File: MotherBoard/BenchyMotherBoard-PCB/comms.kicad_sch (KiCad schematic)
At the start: 0 parts

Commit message: Add MORE regulators, USB, Display, and SDCard
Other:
- company: (none) -> Daxxn Industries
- title: (none) -> Benchy Version 2
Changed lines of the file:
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@@
 (kicad_sch (version 20211123) (generator eeschema)
-  (paper "A4")
+  (paper "A2")
+  (title_block
+    (title "Benchy Version 2")
+    (rev "REV1")
+    (company "Daxxn Industries")
+  )
 )

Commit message: Initial schematic lock
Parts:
- added C? (x4): 10uF, Capacitor_SMD:C_1210_3225Metric, symbol Device:C_Small
- added D? (x6): GP DIODE, Diode_SMD:D_SOD-123, symbol Device:D_Small
- added J?: COMMS-ELOAD, Connector_JST:JST_XA_B04B-XASK-1_1x04_P2.50mm_Vertical, symbol Connector:Conn_01x04_Male
- added J?: COMMS-PWR, Connector_JST:JST_XA_B04B-XASK-1_1x04_P2.50mm_Vertical, symbol Connector:Conn_01x04_Male
- added J?: COMMS-RELAY, Connector_JST:JST_XA_B04B-XASK-1_1x04_P2.50mm_Vertical, symbol Connector:Conn_01x04_Male
- added J?: COMMS-LOGIC, Connector_JST:JST_XA_B04B-XASK-1_1x04_P2.50mm_Vertical, symbol Connector:Conn_01x04_Male
- added K? (x6): JW2SN, Relay_THT:Relay_DPDT_Panasonic_JW2, symbol Daxxn_Relays:JW2SN
- added Q? (x6): MMBT2222A, Package_TO_SOT_SMD:SOT-23, symbol Daxxn_Transistors:MMBT2222A
- added Q? (x6): SSM3K361R_SOT23F, Package_TO_SOT_SMD:SOT-23, symbol Daxxn_Transistors:SSM3K361R_SOT23F
- added R? (x6): 10K, Resistor_SMD:R_0402_1005Metric, symbol Device:R_Small_US
- added R? (x6): 100, Resistor_SMD:R_0402_1005Metric, symbol Device:R_Small_US
- added R? (x6): 1K, Resistor_SMD:R_0402_1005Metric, symbol Device:R_Small_US
- added U?: MAINS-OUT-2, Daxxn_Connectors:AC-EARTH-DIRECT-WIRE, symbol Daxxn_Connectors:3-PIN-AC-DIRECT
- added U?: MAINS-OUT-6, Daxxn_Connectors:AC-EARTH-DIRECT-WIRE, symbol Daxxn_Connectors:3-PIN-AC-DIRECT
- added U?: MAINS-OUT-5, Daxxn_Connectors:AC-EARTH-DIRECT-WIRE, symbol Daxxn_Connectors:3-PIN-AC-DIRECT
- added U?: MAINS-OUT-1, Daxxn_Connectors:AC-EARTH-DIRECT-WIRE, symbol Daxxn_Connectors:3-PIN-AC-DIRECT
- added U?: MAINS-OUT-4, Daxxn_Connectors:AC-EARTH-DIRECT-WIRE, symbol Daxxn_Connectors:3-PIN-AC-DIRECT
- added U?: MAINS-OUT-3, Daxxn_Connectors:AC-EARTH-DIRECT-WIRE, symbol Daxxn_Connectors:3-PIN-AC-DIRECT
- added U?: MAINS-IN, Daxxn_Connectors:AC-EARTH-DIRECT-WIRE, symbol Daxxn_Connectors:3-PIN-AC-DIRECT
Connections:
- new net: Q?.3 (C), R?.1, R?.1 (x6)
- new net: Q?.1 (G), R?.2 (x6)
- new net: D?.2 (A), K?.C-, Q?.3 (D) (x6)
- new net: Q?.2 (B), R?.1 (x6)
- new net: K?.NO2, U?.1 (P) (x6)
- new net: K?.NO1, U?.2 (N) (x6)
- new net: K?.COM1, K?.COM1, K?.COM1, K?.COM1, K?.COM1, K?.COM1, U?.2 (N)
- new net: K?.COM2, K?.COM2, K?.COM2, K?.COM2, K?.COM2, K?.COM2, U?.1 (P)
- new net COMMS.ELOAD-SCK: J?.3 (Pin_3)
- new net COMMS.ELOAD-SDA: J?.2 (Pin_2)
- new net COMMS.LOGIC-SCK: J?.3 (Pin_3)
- new net COMMS.LOGIC-SDA: J?.2 (Pin_2)
- new net COMMS.MAINS-1: R?.2
- new net COMMS.MAINS-2: R?.2
- new net COMMS.MAINS-3: R?.2
- new net COMMS.MAINS-4: R?.2
- new net COMMS.MAINS-5: R?.2
- new net COMMS.MAINS-6: R?.2
- new net COMMS.PWR-SCK: J?.3 (Pin_3)
- new net COMMS.PWR-SDA: J?.2 (Pin_2)
- new net COMMS.RELAY-SCK: J?.3 (Pin_3)
- new net COMMS.RELAY-SDA: J?.2 (Pin_2)
- new net GND: C?.2, C?.2, C?.2, C?.2, J?.4 (Pin_4), J?.4 (Pin_4), J?.4 (Pin_4), J?.4 (Pin_4), Q?.1 (E), Q?.1 (E), Q?.1 (E), Q?.1 (E), Q?.1 (E), Q?.1 (E), Q?.2 (S), Q?.2 (S), Q?.2 (S), Q?.2 (S), Q?.2 (S), Q?.2 (S), U?.3 (E), U?.3 (E), U?.3 (E), U?.3 (E), U?.3 (E), U?.3 (E), U?.3 (E)
- new net VCC: D?.1 (K), D?.1 (K), D?.1 (K), D?.1 (K), D?.1 (K), D?.1 (K), K?.C+, K?.C+, K?.C+, K?.C+, K?.C+, K?.C+, R?.2, R?.2, R?.2, R?.2, R?.2, R?.2
- new net VDD: C?.1, C?.1, C?.1, C?.1, J?.1 (Pin_1), J?.1 (Pin_1), J?.1 (Pin_1), J?.1 (Pin_1)
- no-connect marks 0 -> 12

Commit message: (WIP) Start layout
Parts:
- gave numbers to parts that had none: 57
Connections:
- net VCC: now also K1.8, K2.8, K3.8, K4.8, K5.8, K6.8; no longer K1.C+, K2.C+, K3.C+, K4.C+, K5.C+, K6.C+
- net at D11.2 (A), Q8.3 (D): now also K3.1; no longer K3.C-
- net at D10.2 (A), Q6.3 (D): now also K2.1; no longer K2.C-
- net at U22.1 (P): now also K2.5; no longer K2.NO2
- net at U22.2 (N): now also K2.4; no longer K2.NO1
- net at U26.1 (P): now also K6.5; no longer K6.NO2
- net at U26.2 (N): now also K6.4; no longer K6.NO1
- net at D14.2 (A), Q14.3 (D): now also K6.1; no longer K6.C-
- net at D13.2 (A), Q12.3 (D): now also K5.1; no longer K5.C-
- net at D12.2 (A), Q10.3 (D): now also K4.1; no longer K4.C-
- net at U24.2 (N): now also K4.4; no longer K4.NO1
- net at U24.1 (P): now also K4.5; no longer K4.NO2
- net at U25.2 (N): now also K5.4; no longer K5.NO1
- net at U25.1 (P): now also K5.5; no longer K5.NO2
- net at D9.2 (A), Q4.3 (D): now also K1.1; no longer K1.C-
- net at U20.2 (N): now also K1.4; no longer K1.NO1
- net at U20.1 (P): now also K1.5; no longer K1.NO2
- net at U23.2 (N): now also K3.4; no longer K3.NO1
- net at U23.1 (P): now also K3.5; no longer K3.NO2
- new net: K1.3, K2.3, K3.3, K4.3, K5.3, K6.3, U21.2 (N)
- new net: K1.6, K2.6, K3.6, K4.6, K5.6, K6.6, U21.1 (P)
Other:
- title: Benchy Version 2 -> Benchy Reloaded

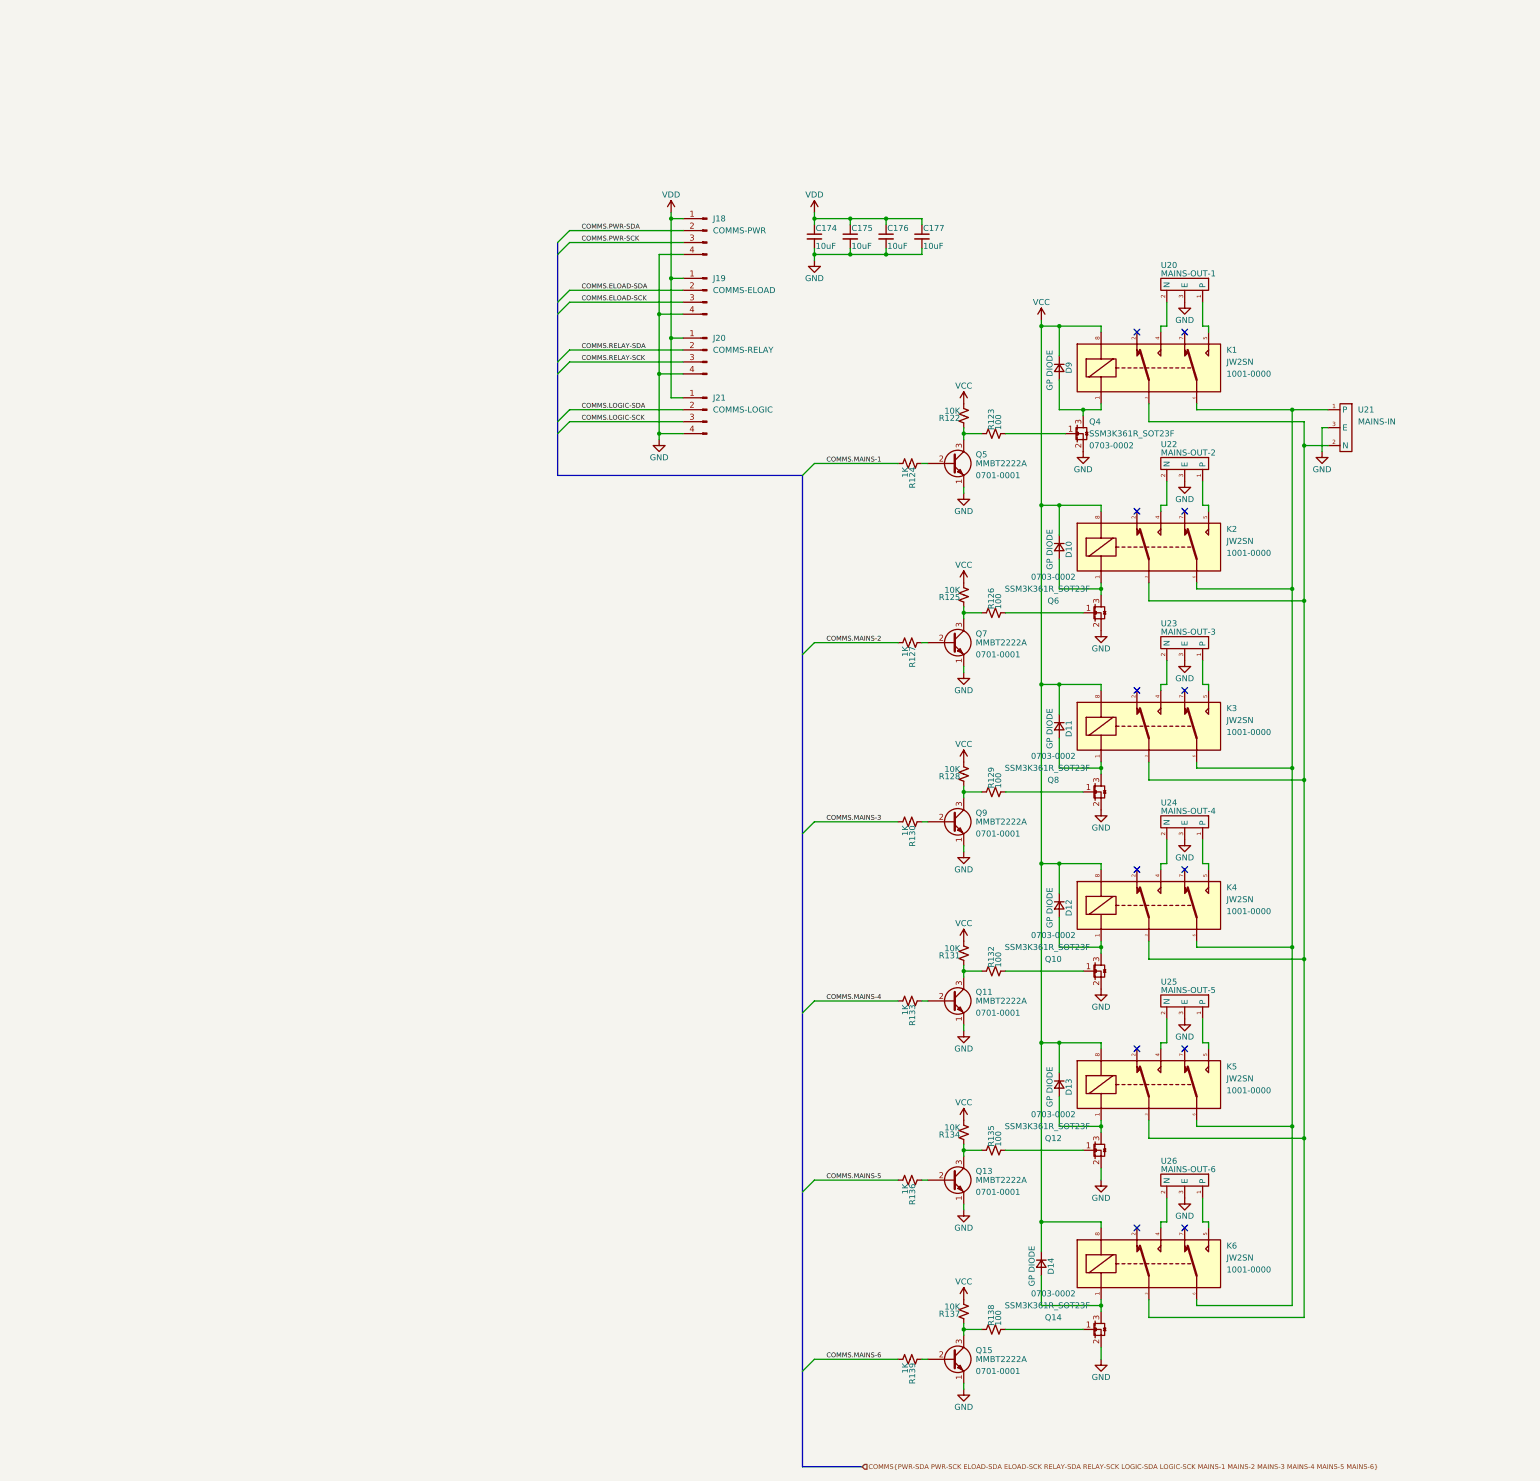
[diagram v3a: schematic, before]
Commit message: (WIP) Replaced DDR VRef with reg and started layout
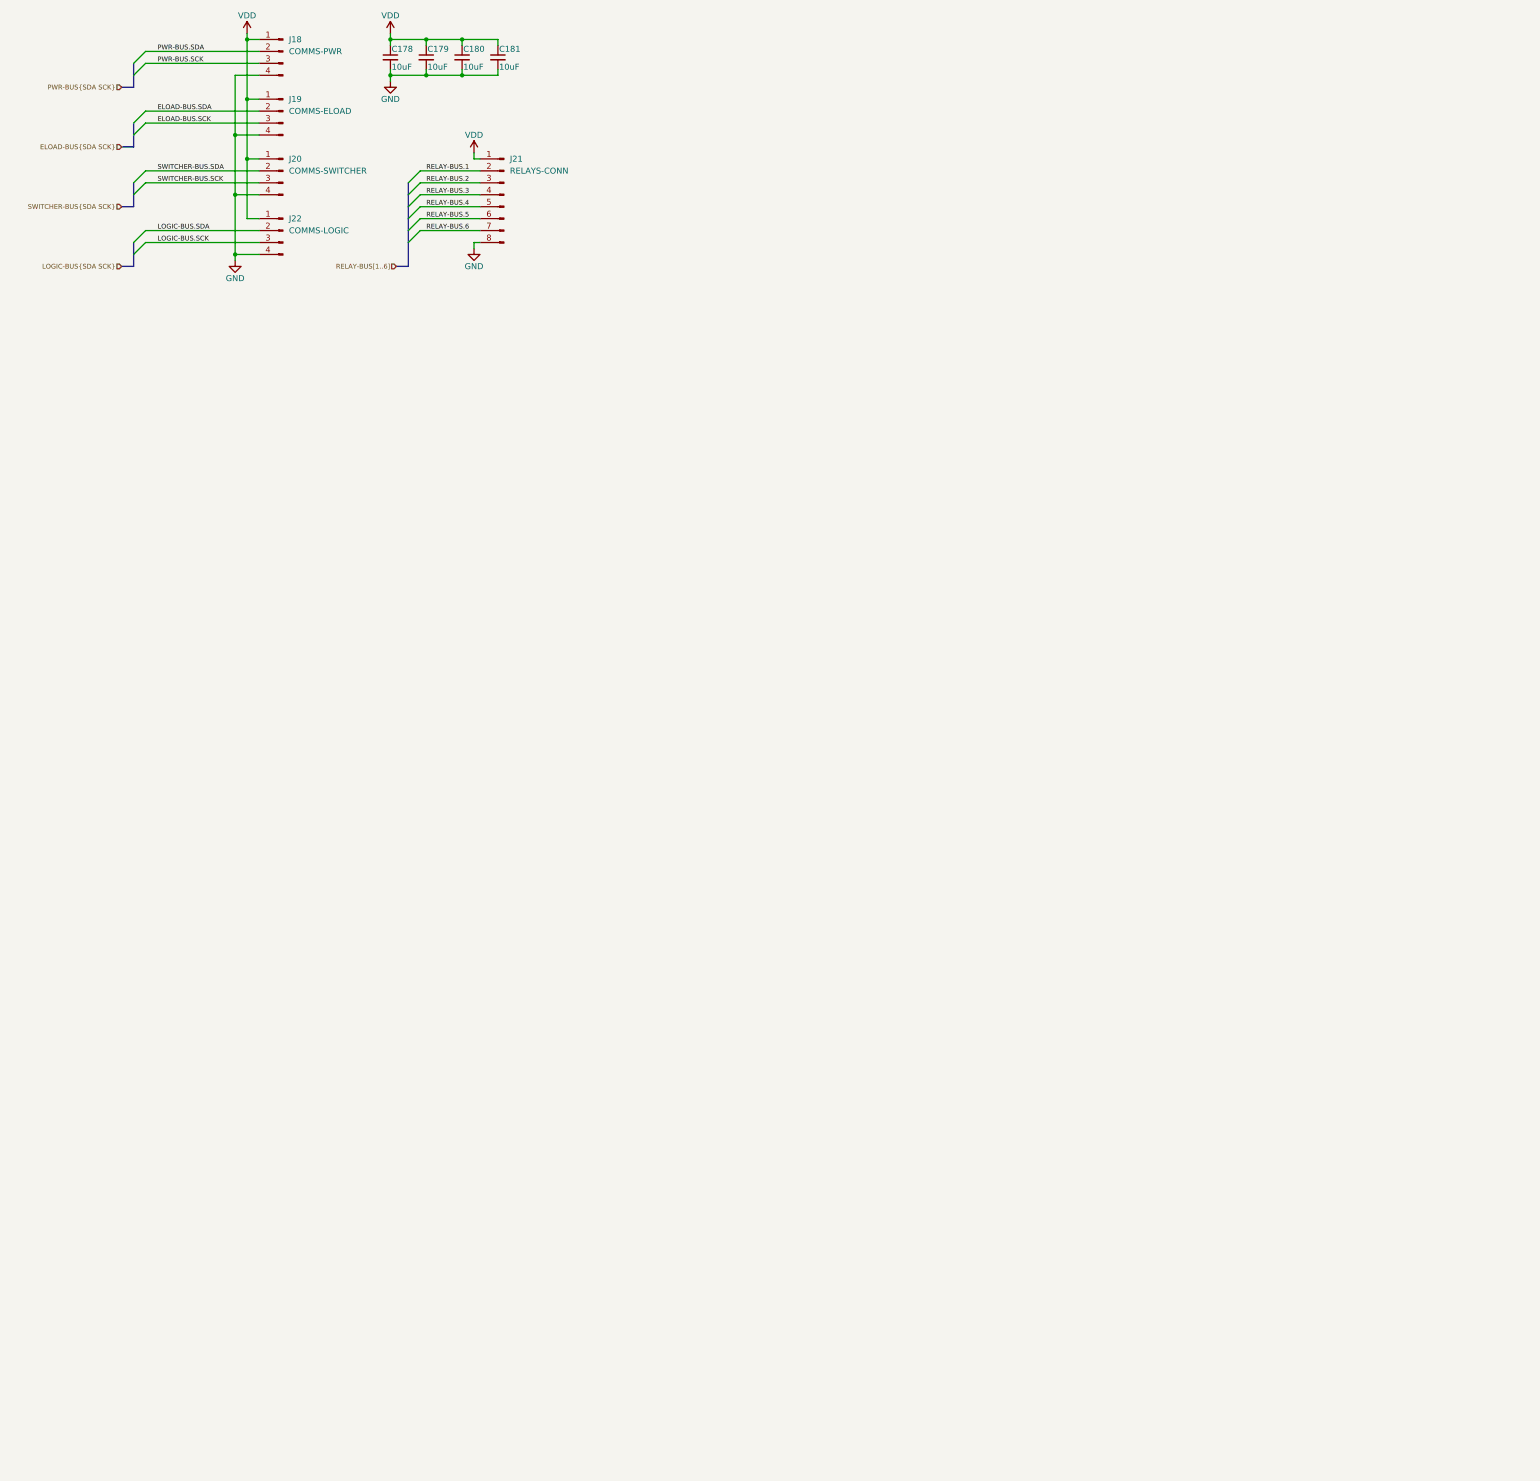
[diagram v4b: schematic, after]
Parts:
- removed D10, D11, D12, D13, D14, D9: GP DIODE, Diode_SMD:D_SOD-123, symbol Device:D_Small
- removed K1, K2, K3, K4, K5, K6: JW2SN, Relay_THT:Relay_DPDT_Panasonic_JW2, symbol Daxxn_Relays:JW2SN
- removed Q10, Q12, Q14, Q4, Q6, Q8: SSM3K361R_SOT23F, Package_TO_SOT_SMD:SOT-23, symbol Daxxn_Transistors:SSM3K361R_SOT23F
- removed Q11, Q13, Q15, Q5, Q7, Q9: MMBT2222A, Package_TO_SOT_SMD:SOT-23, symbol Daxxn_Transistors:MMBT2222A
- removed R122, R125, R128, R131, R134, R137: 10K, Resistor_SMD:R_0402_1005Metric, symbol Device:R_Small_US
- removed R123, R126, R129, R132, R135, R138: 100, Resistor_SMD:R_0402_1005Metric, symbol Device:R_Small_US
- removed R124, R127, R130, R133, R136, R139: 1K, Resistor_SMD:R_0402_1005Metric, symbol Device:R_Small_US
- removed U20: MAINS-OUT-1, Daxxn_Connectors:AC-EARTH-DIRECT-WIRE, symbol Daxxn_Connectors:3-PIN-AC-DIRECT
- removed U21: MAINS-IN, Daxxn_Connectors:AC-EARTH-DIRECT-WIRE, symbol Daxxn_Connectors:3-PIN-AC-DIRECT
- removed U22: MAINS-OUT-2, Daxxn_Connectors:AC-EARTH-DIRECT-WIRE, symbol Daxxn_Connectors:3-PIN-AC-DIRECT
- removed U23: MAINS-OUT-3, Daxxn_Connectors:AC-EARTH-DIRECT-WIRE, symbol Daxxn_Connectors:3-PIN-AC-DIRECT
- removed U24: MAINS-OUT-4, Daxxn_Connectors:AC-EARTH-DIRECT-WIRE, symbol Daxxn_Connectors:3-PIN-AC-DIRECT
- removed U25: MAINS-OUT-5, Daxxn_Connectors:AC-EARTH-DIRECT-WIRE, symbol Daxxn_Connectors:3-PIN-AC-DIRECT
- removed U26: MAINS-OUT-6, Daxxn_Connectors:AC-EARTH-DIRECT-WIRE, symbol Daxxn_Connectors:3-PIN-AC-DIRECT
- added J21: RELAYS-CONN, Connector_JST:JST_XH_B8B-XH-A_1x08_P2.50mm_Vertical, symbol Connector:Conn_01x08_Male
- J18, J19: footprint Connector_JST:JST_XA_B04B-XASK-1_1x04_P2.50mm_Vertical -> Daxxn_Connectors:JST_XH_B4B-XH-A_Vertical
- J20: value COMMS-RELAY -> COMMS-SWITCHER; footprint Connector_JST:JST_XA_B04B-XASK-1_1x04_P2.50mm_Vertical -> Daxxn_Connectors:JST_XH_B4B-XH-A_Vertical
- J22: renamed from J21; footprint Connector_JST:JST_XA_B04B-XASK-1_1x04_P2.50mm_Vertical -> Daxxn_Connectors:JST_XH_B4B-XH-A_Vertical
- renumbered C174 to C178, C175 to C179, C176 to C180, C177 to C181
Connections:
- net GND: now also J21.8 (Pin_8)
- net VDD: now also J21.1 (Pin_1)
- net COMMS.ELOAD-SCK renamed ELOAD-BUS.SCK
- net COMMS.ELOAD-SDA renamed ELOAD-BUS.SDA
- net COMMS.LOGIC-SCK renamed LOGIC-BUS.SCK
- net COMMS.LOGIC-SDA renamed LOGIC-BUS.SDA
- net COMMS.PWR-SCK renamed PWR-BUS.SCK
- net COMMS.PWR-SDA renamed PWR-BUS.SDA
- net COMMS.RELAY-SCK renamed SWITCHER-BUS.SCK
- net COMMS.RELAY-SDA renamed SWITCHER-BUS.SDA
- new net RELAY-BUS.1: J21.2 (Pin_2)
- new net RELAY-BUS.2: J21.3 (Pin_3)
- new net RELAY-BUS.3: J21.4 (Pin_4)
- new net RELAY-BUS.4: J21.5 (Pin_5)
- new net RELAY-BUS.5: J21.6 (Pin_6)
- new net RELAY-BUS.6: J21.7 (Pin_7)
- no-connect marks 12 -> 0
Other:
- moved on the sheet: C178, C179, C180, C181, J18, J19, J20, J22

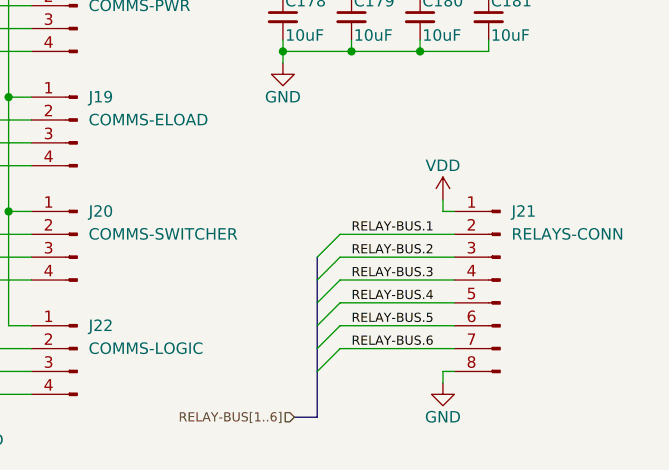
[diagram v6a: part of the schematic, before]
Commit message: Mostly routed USB
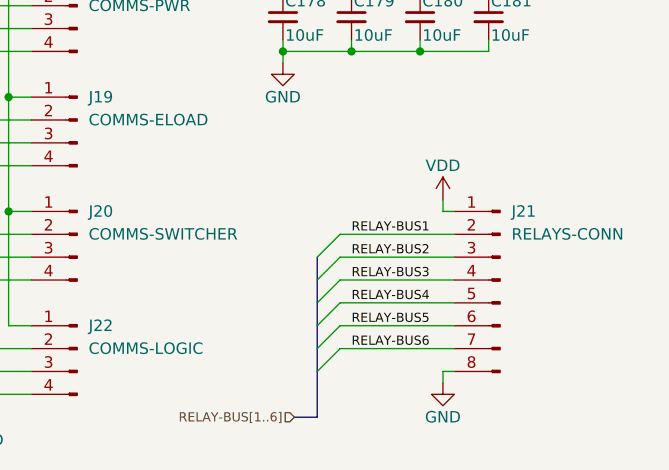
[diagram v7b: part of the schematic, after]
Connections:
- net RELAY-BUS.1 renamed RELAY-BUS1
- net RELAY-BUS.2 renamed RELAY-BUS2
- net RELAY-BUS.3 renamed RELAY-BUS3
- net RELAY-BUS.4 renamed RELAY-BUS4
- net RELAY-BUS.5 renamed RELAY-BUS5
- net RELAY-BUS.6 renamed RELAY-BUS6
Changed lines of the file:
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@@
     (effects (font (size 1.016 1.016)) (justify left bottom))
   )
-  (label "RELAY-BUS.1" (at 110.49 53.34 0) (fields_autoplaced)
+  (label "RELAY-BUS1" (at 110.49 53.34 0) (fields_autoplaced)
     (effects (font (size 1.016 1.016)) (justify left bottom))
   )
@@
     (effects (font (size 1.016 1.016)) (justify left bottom))
   )
-  (label "RELAY-BUS.2" (at 110.49 55.88 0) (fields_autoplaced)
+  (label "RELAY-BUS2" (at 110.49 55.88 0) (fields_autoplaced)
     (effects (font (size 1.016 1.016)) (justify left bottom))
   )
@@
     (effects (font (size 1.016 1.016)) (justify left bottom))
   )
-  (label "RELAY-BUS.5" (at 110.49 63.5 0) (fields_autoplaced)
+  (label "RELAY-BUS5" (at 110.49 63.5 0) (fields_autoplaced)
     (effects (font (size 1.016 1.016)) (justify left bottom))
   )
-  (label "RELAY-BUS.4" (at 110.49 60.96 0) (fields_autoplaced)
+  (label "RELAY-BUS4" (at 110.49 60.96 0) (fields_autoplaced)
     (effects (font (size 1.016 1.016)) (justify left bottom))
   )
-  (label "RELAY-BUS.3" (at 110.49 58.42 0) (fields_autoplaced)
+  (label "RELAY-BUS3" (at 110.49 58.42 0) (fields_autoplaced)
     (effects (font (size 1.016 1.016)) (justify left bottom))
   )
-  (label "RELAY-BUS.6" (at 110.49 66.04 0) (fields_autoplaced)
+  (label "RELAY-BUS6" (at 110.49 66.04 0) (fields_autoplaced)
     (effects (font (size 1.016 1.016)) (justify left bottom))
   )
